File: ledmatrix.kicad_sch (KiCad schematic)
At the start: 1 part

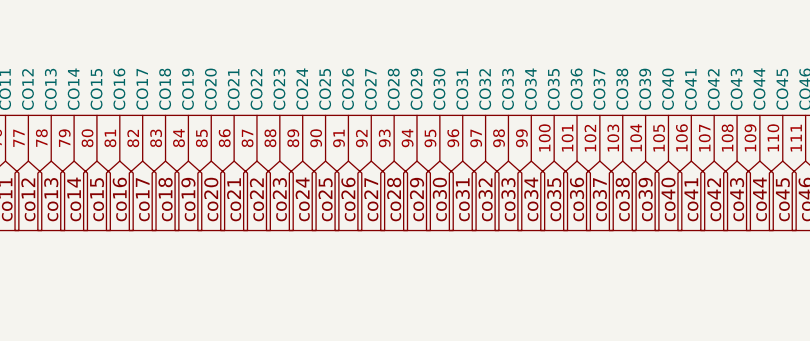
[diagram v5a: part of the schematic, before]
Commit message: Added a schematic comments; I don't know why other files are updated
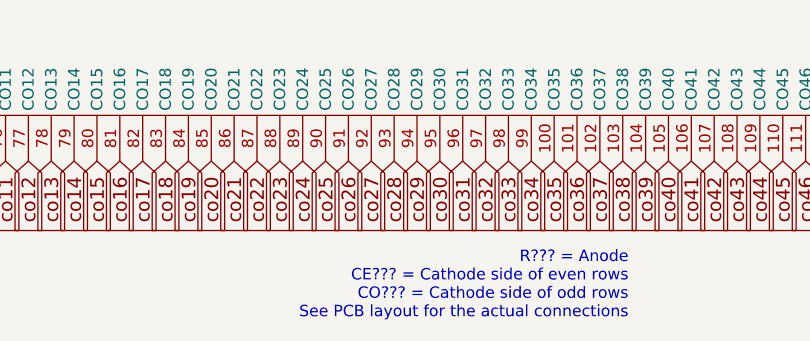
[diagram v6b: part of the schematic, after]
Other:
- note added: "R??? = Anode CE??? = Cathode side of even rows CO??? = Cathode side of odd rows See PCB layout for the actual connections"
